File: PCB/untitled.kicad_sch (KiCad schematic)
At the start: 8 parts, among them U9 XC7A100T-CSG324

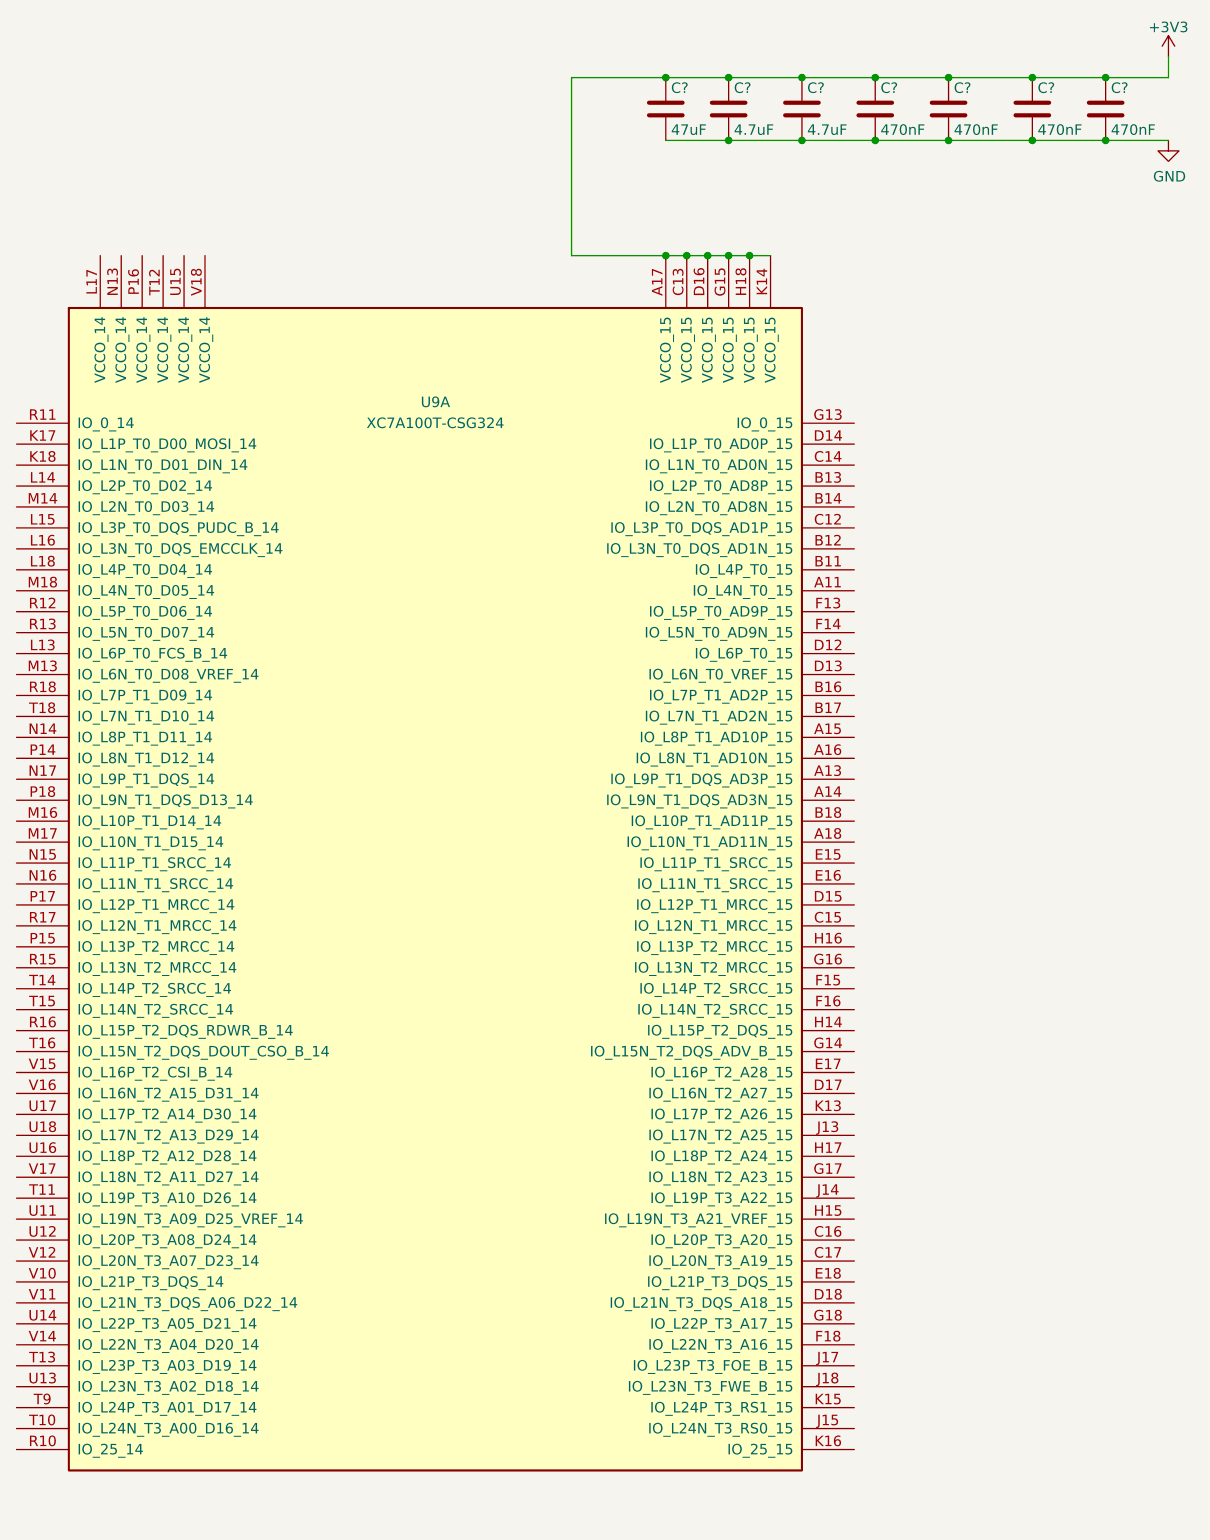
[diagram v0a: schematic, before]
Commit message: add usb micro and switches
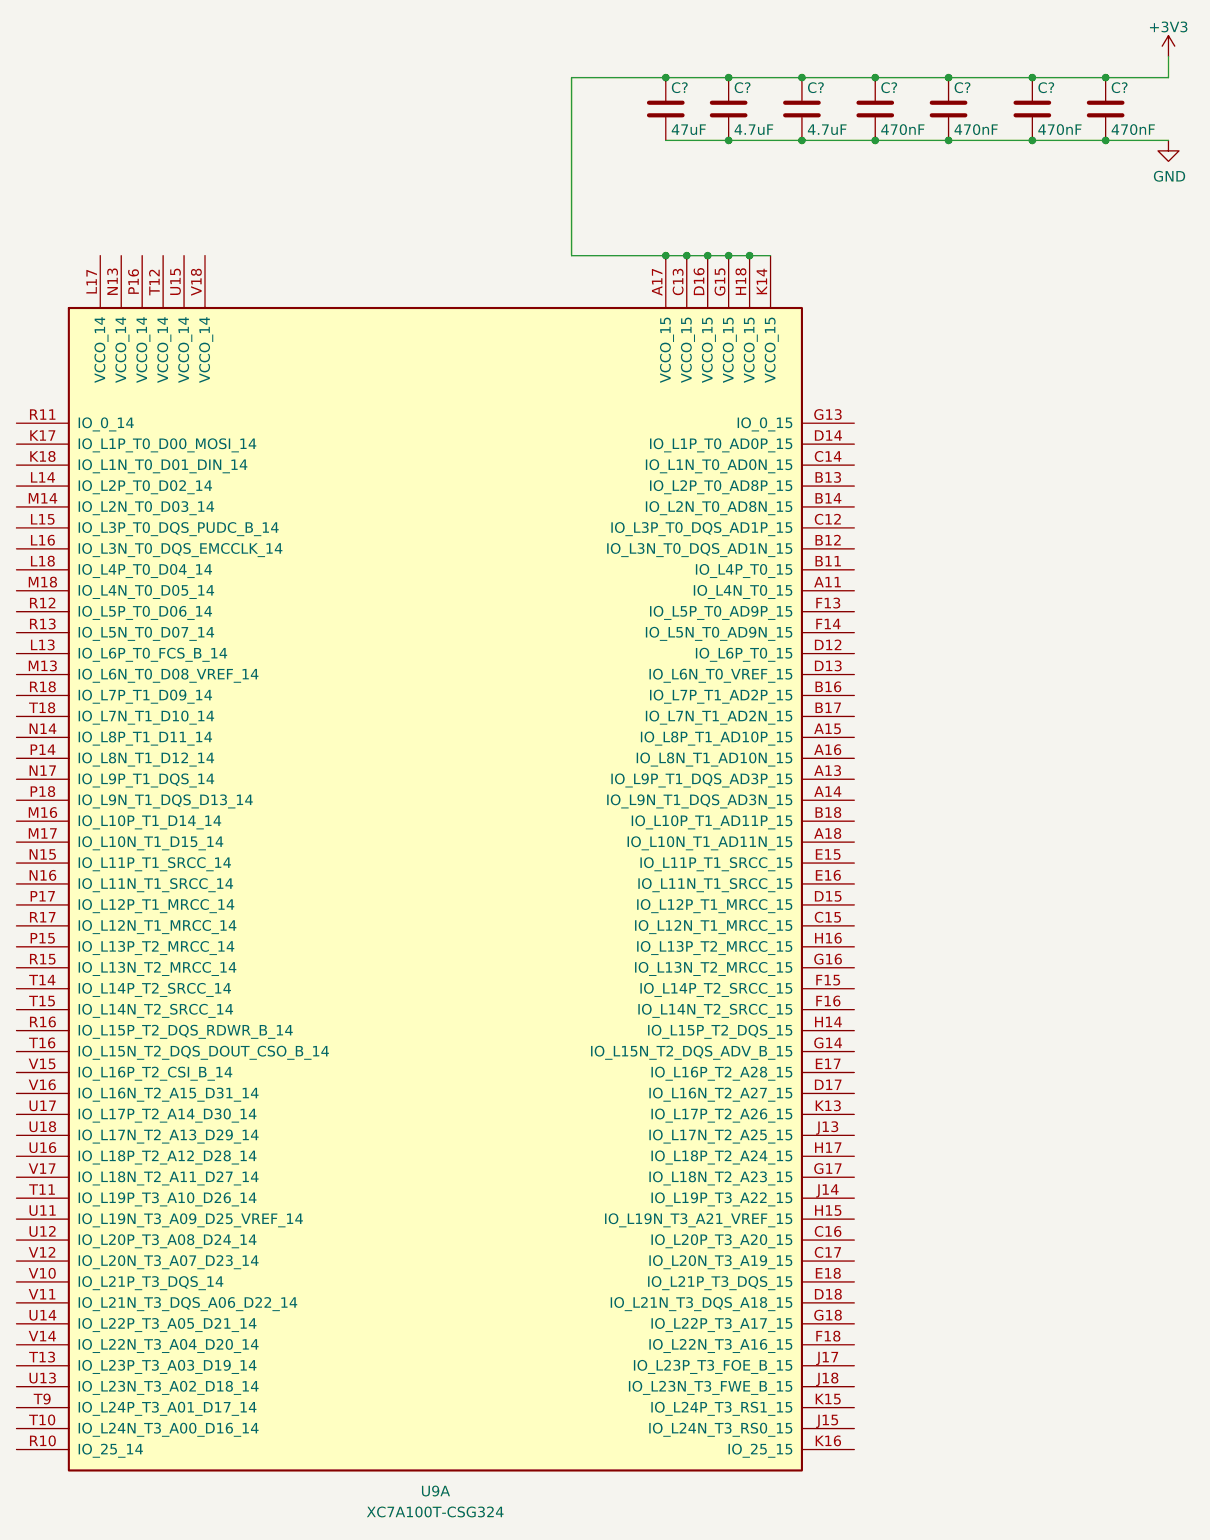
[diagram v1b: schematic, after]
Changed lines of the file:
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@@
   (symbol (lib_id "FPGA_Xilinx_Artix7:XC7A100T-CSG324") (at 64.77 116.84 0) (unit 1)
     (in_bom yes) (on_board yes) (dnp no) (fields_autoplaced)
-    (property "Reference" "U9" (at 64.77 60.96 0)
+    (property "Reference" "U9" (at 64.77 193.04 0)
       (effects (font (size 1.27 1.27)))
     )
-    (property "Value" "XC7A100T-CSG324" (at 64.77 63.5 0)
+    (property "Value" "XC7A100T-CSG324" (at 64.77 195.58 0)
       (effects (font (size 1.27 1.27)))
     )
